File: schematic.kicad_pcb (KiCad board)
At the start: 4 copper layers, 66 x 48.3 mm, 60 parts, among them J2 Audio Out, J4 Audio In, Q2 2N5457 (JFET), Q3 2N5457 (JFET), Q4 2N5457 (JFET), Q5 2N5457 (JFET), Q6 2N3904, Q7 2N3904, Q8 2N3904, SW1 SW_SPST, U1 LM741, U2 LM741, U3 LM741, U4 LM741, U5 LM741

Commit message: update
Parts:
- removed C13: 10µF, Capacitor_THT:CP_Radial_D5.0mm_P2.50mm
- removed J2: Audio Out, Library:AudioMountPoint2
- removed Q8: 2N3904, Package_TO_SOT_THT:TO-92_Inline_Wide
- added C14: 10µF, Capacitor_THT:CP_Radial_D5.0mm_P2.50mm, F.Cu at (113.7, 119.4)
- added J1: Audio Out, Connector_PinHeader_2.54mm:PinHeader_1x02_P2.54mm_Vertical, F.Cu at (61.5, 114.9)
- added Q1: 2N3904, Package_TO_SOT_THT:TO-92_Inline, F.Cu at (77.5, 114.9)
- added R28: 56K, Resistor_THT:R_Axial_DIN0204_L3.6mm_D1.6mm_P5.08mm_Horizontal, F.Cu at (108.0, 101.6)
- added R29: 3.9K, Resistor_THT:R_Axial_DIN0204_L3.6mm_D1.6mm_P5.08mm_Horizontal, F.Cu at (102.9, 104.1)
- added R30: 39K, Resistor_THT:R_Axial_DIN0204_L3.6mm_D1.6mm_P5.08mm_Horizontal, F.Cu at (109.9, 101.6)
- added R31: 1K, Resistor_THT:R_Axial_DIN0204_L3.6mm_D1.6mm_P5.08mm_Horizontal, F.Cu at (114.9, 104.1)
- BT1, SW1: footprint LED_THT:LED_D2.0mm_W4.8mm_H2.5mm_FlatTop -> Connector_PinHeader_2.54mm:PinHeader_1x02_P2.54mm_Vertical
- C1, C2, C3, C4: footprint Resistor_THT:R_Axial_DIN0207_L6.3mm_D2.5mm_P7.62mm_Horizontal -> Capacitor_THT:C_Axial_L5.1mm_D3.1mm_P7.50mm_Horizontal
- C10: value 22µF -> 220µF; footprint Capacitor_THT:CP_Radial_D5.0mm_P2.50mm -> Capacitor_THT:CP_Radial_D10.0mm_P5.00mm
- C11, C5, C6, C7: footprint Resistor_THT:R_Axial_DIN0207_L6.3mm_D2.5mm_P5.08mm_Vertical -> Capacitor_THT:C_Disc_D3.0mm_W1.6mm_P2.50mm
- C12, C8: footprint Resistor_THT:R_Axial_DIN0207_L6.3mm_D2.5mm_P5.08mm_Vertical -> Capacitor_THT:C_Axial_L5.1mm_D3.1mm_P7.50mm_Horizontal
- C9: value 220µF -> 22µF; footprint Capacitor_THT:CP_Radial_D10.0mm_P5.00mm -> Capacitor_THT:CP_Radial_D5.0mm_P2.50mm
- D1: footprint Resistor_THT:R_Axial_DIN0207_L6.3mm_D2.5mm_P5.08mm_Vertical -> Diode_THT:D_A-405_P7.62mm_Horizontal
- J4: footprint Library:AudioMountPoint2 -> Connector_PinHeader_2.54mm:PinHeader_1x03_P2.54mm_Vertical
- Q2, Q3, Q4, Q5, Q6, Q7: footprint Package_TO_SOT_THT:TO-92_Inline_Wide -> Package_TO_SOT_THT:TO-92_Inline
- R1, R10, R11, R12, R14, R2, R22, R23, R26, R3, R4, R5, R6, R7, R8, R9: footprint Resistor_THT:R_Axial_DIN0207_L6.3mm_D2.5mm_P7.62mm_Horizontal -> Resistor_THT:R_Axial_DIN0204_L3.6mm_D1.6mm_P5.08mm_Horizontal
- R13, R15: footprint Resistor_THT:R_Axial_DIN0207_L6.3mm_D2.5mm_P5.08mm_Vertical -> Resistor_THT:R_Axial_DIN0204_L3.6mm_D1.6mm_P5.08mm_Horizontal
- R16: value 2.2K -> 22K; footprint Resistor_THT:R_Axial_DIN0207_L6.3mm_D2.5mm_P2.54mm_Vertical -> Resistor_THT:R_Axial_DIN0204_L3.6mm_D1.6mm_P5.08mm_Horizontal
- R17: value 22K -> 47K; footprint Resistor_THT:R_Axial_DIN0207_L6.3mm_D2.5mm_P2.54mm_Vertical -> Resistor_THT:R_Axial_DIN0204_L3.6mm_D1.6mm_P5.08mm_Horizontal
- R18, R27: footprint Resistor_THT:R_Axial_DIN0207_L6.3mm_D2.5mm_P2.54mm_Vertical -> Resistor_THT:R_Axial_DIN0204_L3.6mm_D1.6mm_P5.08mm_Horizontal
- R19: value 47K -> 2.2K; footprint Resistor_THT:R_Axial_DIN0207_L6.3mm_D2.5mm_P2.54mm_Vertical -> Resistor_THT:R_Axial_DIN0204_L3.6mm_D1.6mm_P5.08mm_Horizontal
- R20: value 390K -> 330K; footprint Resistor_THT:R_Axial_DIN0207_L6.3mm_D2.5mm_P7.62mm_Horizontal -> Resistor_THT:R_Axial_DIN0204_L3.6mm_D1.6mm_P5.08mm_Horizontal
- R21: value 510K -> 470K; footprint Resistor_THT:R_Axial_DIN0207_L6.3mm_D2.5mm_P7.62mm_Horizontal -> Resistor_THT:R_Axial_DIN0204_L3.6mm_D1.6mm_P5.08mm_Horizontal
- R24: value 150K -> 510K; footprint Resistor_THT:R_Axial_DIN0207_L6.3mm_D2.5mm_P2.54mm_Vertical -> Resistor_THT:R_Axial_DIN0204_L3.6mm_D1.6mm_P5.08mm_Horizontal
- R25: value 510K -> 150K; footprint Resistor_THT:R_Axial_DIN0207_L6.3mm_D2.5mm_P2.54mm_Vertical -> Resistor_THT:R_Axial_DIN0204_L3.6mm_D1.6mm_P5.08mm_Horizontal
- RV1, RV2: footprint Potentiometer_THT:Potentiometer_Bourns_3266Y_Vertical -> Connector_PinHeader_2.54mm:PinHeader_1x02_P2.54mm_Vertical
- RV3: footprint Potentiometer_THT:Potentiometer_Runtron_RM-065_Vertical -> Potentiometer_THT:Potentiometer_Runtron_RM-063_Horizontal
- moved Q6 123.2 mm to (34.9, 116.8), turned to 90 degrees
- moved R27 115.2 mm to (38.7, 119.4), turned to 90 degrees
- moved C7 114.7 mm to (41.8, 116.8), turned to 90 degrees
- moved U1 114.0 mm to (41.9, 94.0)
- moved C8 111.8 mm to (41.9, 122.6)
- moved J4 111.8 mm to (48.3, 113.0)
- moved R14 111.1 mm to (44.5, 125.7)
- moved R15 109.8 mm to (44.5, 121.9), turned to 90 degrees
- moved C1 107.7 mm to (41.3, 90.2), turned to 180 degrees
- moved R3 102.4 mm to (48.3, 106.7)
- moved R1 101.0 mm to (50.8, 89.5), turned to 180 degrees
- moved Q2 95.8 mm to (34.3, 106.0), turned to 0 degrees
- moved C2 88.8 mm to (46.4, 99.7), turned to 90 degrees
- moved C5 86.9 mm to (55.8, 115.6), turned to 180 degrees
- moved R4 86.1 mm to (53.3, 89.5), turned to 0 degrees
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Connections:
- net Net-(C6-Pad1) renamed A_WET
- BT1 pad 1: Net-(BT1-+) -> +9V
- C1 pad 1: Net-(Q6-E) -> A_DRY
- C1 pad 2: Net-(Q2-D) -> Net-(U1-+)
- C10 pad 1: Net-(Q2-G) -> +7V
- C11 pad 2: Net-(Q2-S) -> LFO_OUT1
- C2 pad 1: Net-(C2-Pad1) -> Net-(Q3-D)
- C2 pad 2: Net-(Q3-D) -> Net-(U2-+)
- C3 pad 1: Net-(C3-Pad1) -> Net-(Q4-D)
- C3 pad 2: Net-(Q4-D) -> Net-(U3-+)
- C4 pad 1: Net-(C4-Pad1) -> Net-(Q5-D)
- C4 pad 2: Net-(Q5-1D) -> Net-(U4-+)
- C5 pad 2: Net-(Q6-E) -> A_DRY
- C7 pad 2: Net-(C7-Pad2) -> Net-(J4-T)
- C8 pad 1: Net-(Q6-B) -> GND
- C8 pad 2: Net-(BT1--) -> Net-(Q6-B)
- C9 pad 1: Net-(Q6-C) -> +4V
- Q2 pad 1: Net-(Q2-D) -> A_DRY
- Q2 pad 2: Net-(Q2-G) -> 4V
- Q2 pad 3: Net-(Q2-S) -> LFO_OUT1
- Q3 pad 2: Net-(Q2-G) -> 4V
- Q3 pad 3: Net-(Q2-S) -> LFO_OUT1
- Q4 pad 2: Net-(Q2-G) -> 4V
- Q4 pad 3: Net-(Q2-S) -> LFO_OUT1
- Q5 pad 1: Net-(Q5-1D) -> Net-(Q5-D)
- Q5 pad 2: Net-(Q2-G) -> 4V
- Q5 pad 3: Net-(Q2-S) -> LFO_OUT1
- Q6 pad 1: Net-(Q6-E) -> A_DRY
- Q6 pad 3: Net-(Q6-C) -> +7V
- Q7 pad 1: Net-(Q2-G) -> +7V
- Q7 pad 2: Net-(Q7-B) -> Net-(D1-K)
- Q7 pad 3: Net-(Q6-C) -> +9V
- R1 pad 1: Net-(Q6-E) -> A_DRY
- R13 pad 1: Net-(Q2-G) -> 4V
- R14 pad 1: Net-(Q6-E) -> GND
- R14 pad 2: Net-(BT1--) -> A_DRY
- R15 pad 1: Net-(Q6-B) -> GND
- R15 pad 2: Net-(BT1--) -> Net-(Q6-B)
- R16 pad 1: Net-(BT1-+) -> +4V
- R16 pad 2: Net-(D1-K) -> GND
- R17 pad 1: Net-(Q6-C) -> Net-(Q1-B)
- R17 pad 2: Net-(Q7-B) -> GND
- R18 pad 1: Net-(Q2-G) -> +7V
- R18 pad 2: GND -> Net-(Q1-B)
- R19 pad 1: Net-(Q7-B) -> +9V
- R19 pad 2: GND -> Net-(D1-K)
- R20 pad 1: Net-(Q2-S) -> Net-(R20-Pad1)
- R21 pad 2: Net-(Q2-S) -> LFO_OUT1
- R22 pad 1: Net-(C13-Pad1) -> Net-(R22-Pad1)
- R22 pad 2: Net-(R21-Pad1) -> Net-(C14-Pad1)
- R23 pad 2: Net-(Q2-G) -> +4V
- R24 pad 1: Net-(C13-Pad1) -> Net-(U5-+)
- R24 pad 2: Net-(U5--) -> Net-(C12-Pad2)
- R25 pad 1: Net-(U5-+) -> Net-(C14-Pad1)
- R25 pad 2: Net-(C12-Pad2) -> Net-(U5--)
- R26 pad 2: Net-(C12-Pad2) -> Net-(R26-Pad2)
- R27 pad 1: Net-(Q6-C) -> Net-(Q6-B)
- R27 pad 2: Net-(Q6-B) -> +7V
- R3 pad 2: Net-(C2-Pad1) -> Net-(Q3-D)
- R4 pad 1: Net-(C2-Pad1) -> Net-(Q3-D)
- R5 pad 2: Net-(C3-Pad1) -> Net-(Q4-D)
- R6 pad 1: Net-(C3-Pad1) -> Net-(Q4-D)
- R7 pad 2: Net-(C4-Pad1) -> Net-(Q5-D)
- R8 pad 1: Net-(C4-Pad1) -> Net-(Q5-D)
- RV2 pad 1: unconnected-(RV2-Pad1) -> Net-(R22-Pad1)
- RV3 pad 1: Net-(Q2-G) -> +4V
- U1 pad 3: Net-(Q2-D) -> Net-(U1-+)
- U1 pad 6: Net-(C2-Pad1) -> Net-(Q3-D)
- U1 pad 7: Net-(Q6-C) -> +7V
- U2 pad 3: Net-(Q3-D) -> Net-(U2-+)
- U2 pad 6: Net-(C3-Pad1) -> Net-(Q4-D)
- U2 pad 7: Net-(Q6-C) -> +7V
- U3 pad 3: Net-(Q4-D) -> Net-(U3-+)
- U3 pad 6: Net-(C4-Pad1) -> Net-(Q5-D)
- U3 pad 7: Net-(Q6-C) -> +7V
- U4 pad 3: Net-(Q5-1D) -> Net-(U4-+)
- U4 pad 7: Net-(Q6-C) -> +7V
- U5 pad 6: Net-(C12-Pad2) -> Net-(R26-Pad2)
- U5 pad 7: Net-(Q2-G) -> +4V
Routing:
- net GND: track 176.6 -> 0.00 mm, vias 2 -> 0
- net Net-(Q2-G): track 106.8 -> 0.00 mm, vias 4 -> 0
- net Net-(Q6-C): track 98.7 -> 0.00 mm, vias 4 -> 0
- net Net-(Q2-D): track 74.0 -> 0.00 mm, vias 2 -> 0
- net Net-(U5-+): track 72.2 -> 0.00 mm, vias 6 -> 0
- net Net-(Q3-D): track 62.4 -> 0.00 mm, vias 3 -> 0
- net Net-(Q2-S): track 58.9 -> 0.00 mm, vias 2 -> 0
- net Net-(Q4-D): track 50.9 -> 0.00 mm, vias 2 -> 0
- net Net-(Q6-E): track 50.4 -> 0.00 mm, vias 3 -> 0
- net Net-(Q5-1D): track 48.4 -> 0.00 mm, vias 2 -> 0
- net A_WET: track 47.9 -> 0.00 mm, vias 5 -> 0
- net Net-(R26-Pad1): track 44.1 -> 0.00 mm, vias 3 -> 0
- net Net-(R20-Pad2): track 40.2 -> 0.00 mm, vias 2 -> 0
- net Net-(U5--): track 37.6 -> 0.00 mm, vias 2 -> 0
- net Net-(C3-Pad1): track 36.6 -> 0.00 mm, vias 5 -> 0
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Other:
- board size 66 x 48.3 mm -> 86.4 x 43.2 mm
- copper layers 4 -> 2
- board text added: "All-Pass Filter"
- board text added: "CAN'T PHASE ME V1.0: PCB BY 42 BERLIN SYNTHLAB"
- board text added: "FS Mix"
- board text added: "JLCJLCJLCJLC"
- board text added: "LFO"
- board text added: "ORIGINAL CIRCUIT: https://www.instructables.com/Phaser-Guitar-Pedal/"
- board text added: "Preamp"
- board text added: "Voltage Divider"
- board text added: "github.com/ fablabnk/ SynthLabProjects"

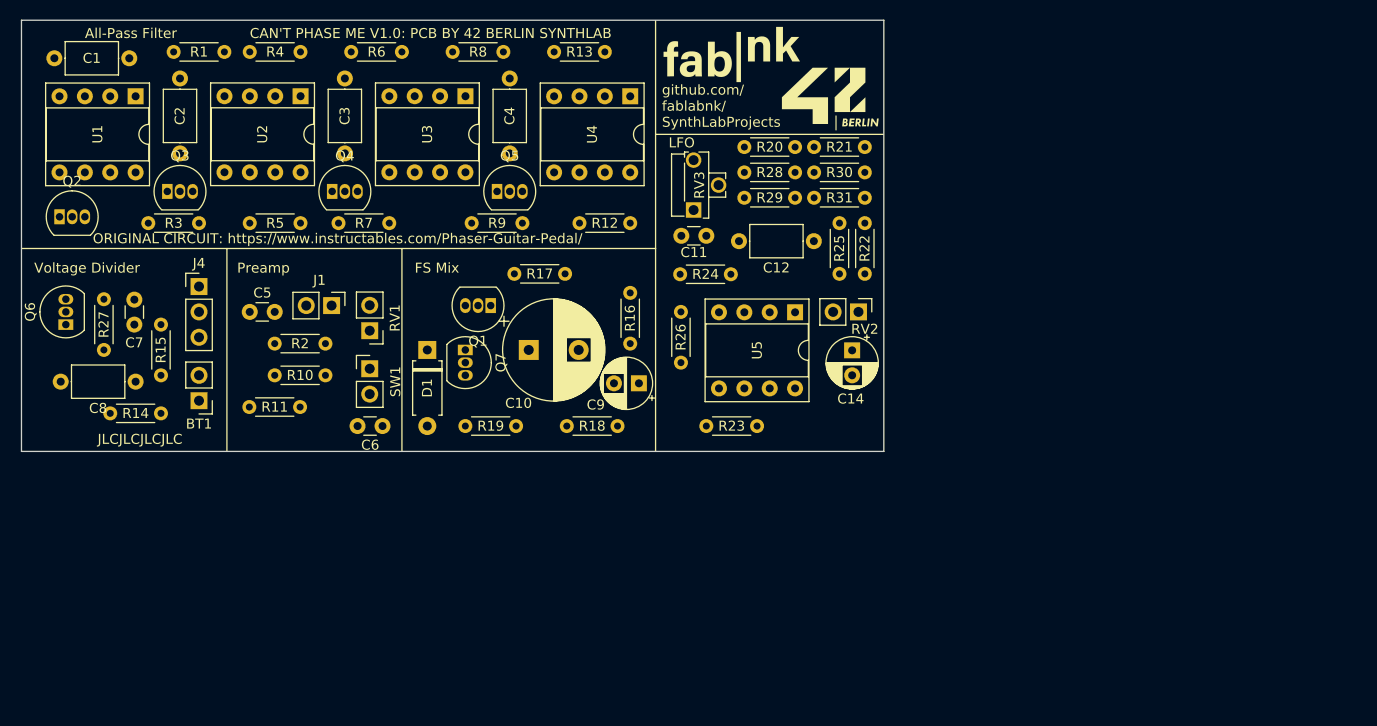
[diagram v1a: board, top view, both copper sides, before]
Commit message: smaller redesign - ready to test laser cut
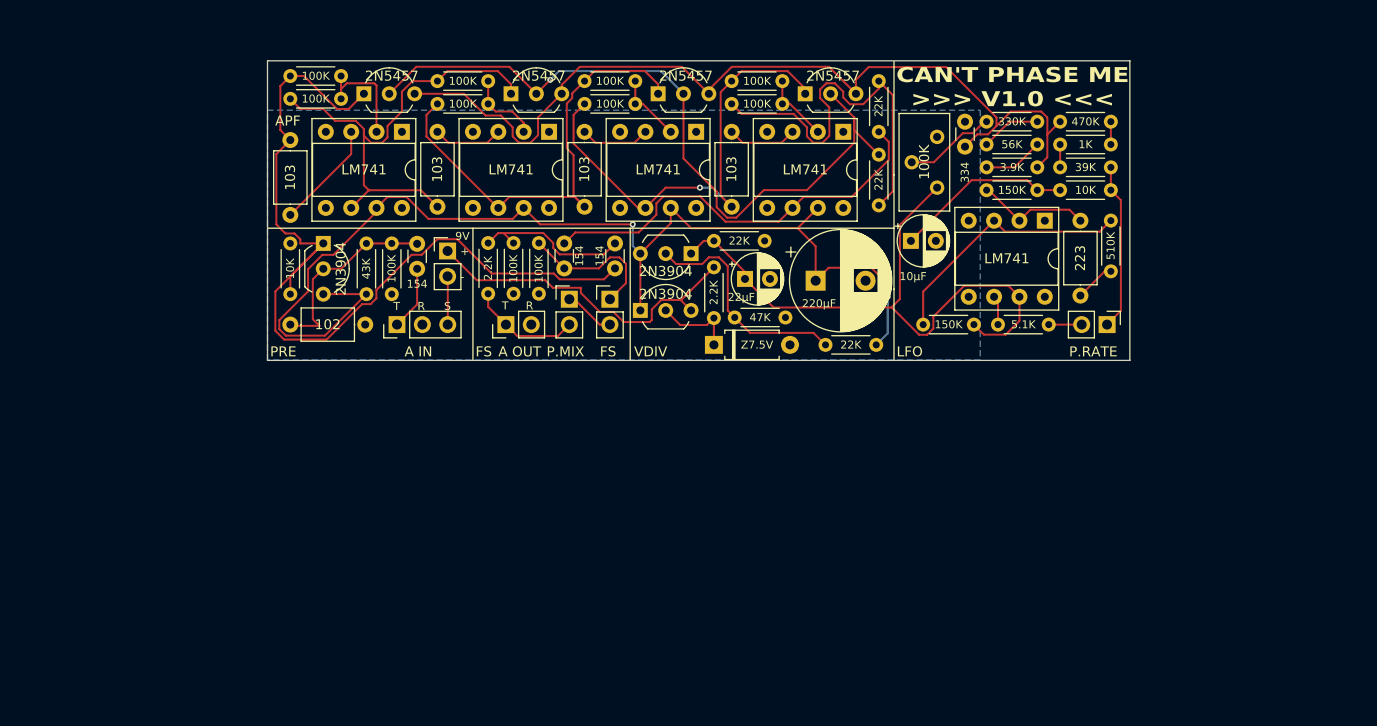
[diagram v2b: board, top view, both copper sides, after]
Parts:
- removed J4: Audio In, Connector_PinHeader_2.54mm:PinHeader_1x03_P2.54mm_Vertical
- removed SW1: SW_SPST, Connector_PinHeader_2.54mm:PinHeader_1x02_P2.54mm_Vertical
- added J2: AudioJack3, Library:PinHeader_1x03_P2.54mm_Vertical_TRS, F.Cu at (68.1, 116.8)
- added SW2: SW_DPDT_x2, Library:PinHeader_1x02_P2.54mm_Vertical_2_3, F.Cu at (89.4, 114.3)
- BT1: value 9V -> 9V Battery
- D1: value D_Zener 7.5V -> Z7.5V
- J1: value Audio Out -> AudioJack3; footprint Connector_PinHeader_2.54mm:PinHeader_1x02_P2.54mm_Vertical -> Library:PinHeader_1x02_P2.54mm_Vertical_TR
- Q1, Q6, Q7: footprint Package_TO_SOT_THT:TO-92_Inline -> Package_TO_SOT_THT:TO-92_Inline_Wide
- Q2, Q3, Q4, Q5: value 2N5457 (JFET) -> 2N5457; footprint Package_TO_SOT_THT:TO-92_Inline -> Package_TO_SOT_THT:TO-92_Inline_Wide
- RV3: footprint Potentiometer_THT:Potentiometer_Runtron_RM-063_Horizontal -> Potentiometer_THT:Potentiometer_Bourns_3296Y_Vertical
- moved R24 43.5 mm to (139.6, 106.4), turned to -90 degrees
- moved R26 36.9 mm to (133.3, 116.8), turned to 180 degrees
- moved Q3 35.8 mm to (79.5, 93.7)
- moved C5 34.8 mm to (89.9, 108.7), turned to -90 degrees
- moved R13 34.1 mm to (116.3, 99.8), turned to -90 degrees
- moved Q4 34.1 mm to (94.2, 93.7)
- moved R11 33.3 mm to (82.3, 108.7), turned to -90 degrees
- moved Q2 32.9 mm to (64.8, 93.7)
- moved Q5 32.4 mm to (109.0, 93.7)
- moved R18 32.0 mm to (116.1, 118.9), turned to 180 degrees
- moved R7 32.0 mm to (91.9, 94.7), turned to 180 degrees
- moved C10 29.6 mm to (110.0, 112.4)
- moved R19 29.5 mm to (99.8, 111.1), turned to -90 degrees
- moved R29 29.5 mm to (132.2, 101.1), turned to 180 degrees
- moved C7 29.5 mm to (70.1, 108.8), turned to -90 degrees
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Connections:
- R2 pad 1: Net-(J1-T) -> Net-(J1-PadT)
- RV1 pad 2: Net-(J1-T) -> Net-(J1-PadT)
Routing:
- net +7V: track 0.00 -> 112.2 mm, vias 0 -> 2
- net LFO_OUT1: track 0.00 -> 91.2 mm
- net A_DRY: track 0.00 -> 89.7 mm
- net 4V: track 0.00 -> 74.3 mm, vias 0 -> 1
- net +4V: track 0.00 -> 62.7 mm
- net Net-(Q5-D): track 0.00 -> 47.1 mm, vias 0 -> 1
- net Net-(Q3-D): track 0.00 -> 46.9 mm
- net Net-(Q4-D): track 0.00 -> 46.7 mm
- net A_WET: track 0.00 -> 41.9 mm
- net Net-(R12-Pad1): track 0.00 -> 39.6 mm
- net +9V: track 0.00 -> 34.3 mm
- net Net-(U5-+): track 0.00 -> 26.0 mm
- net Net-(Q1-B): track 0.00 -> 23.0 mm
- net Net-(Q6-B): track 0.00 -> 19.9 mm
- net Net-(C14-Pad1): track 0.00 -> 17.9 mm
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- added copper zone on B.Cu, net GND
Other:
- board size 86.4 x 43.2 mm -> 86.4 x 30 mm
- board text added: "+"
- board text added: "-"
- board text added: "9V"
- board text added: "A IN"
- board text added: "A OUT"
- board text added: "APF"
- board text added: "CAN'T PHASE ME >>> V1.0 <<<"
- board text added: "FS"
- board text added: "Lab"
- board text added: "P.MIX"
- board text added: "P.RATE"
- board text added: "PRE"
- board text added: "R"
- board text added: "S"
- board text added: "T"
- board text added: "VDIV"
- board text added: "https://github.com/fablabnk/SynthLabProjects"
- board text added: "pedal"
- board text removed: "All-Pass Filter"
- board text removed: "CAN'T PHASE ME V1.0: PCB BY 42 BERLIN SYNTHLAB"
- board text removed: "FS Mix"
- board text removed: "Preamp"
- board text removed: "Voltage Divider"
- board text removed: "github.com/ fablabnk/ SynthLabProjects"
